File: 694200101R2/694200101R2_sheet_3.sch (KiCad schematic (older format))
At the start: 48 parts

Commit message: Updated Schematic to use KiCad LED Driver Symbols
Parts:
- added C18, C20, C21, C22: 0.47uF, Capacitor_SMD:C_0603_1608Metric, symbol Device:C
- added C19: 22uF, capacitor-lib:CAPPC3528X210N, symbol Device:CP1
- added C23, C24, C27: 100nF, Capacitor_SMD:C_0603_1608Metric, symbol Device:C
- added R11: 59k, Resistor_SMD:R_2512_6332Metric, symbol Device:R_US
- added R15, R16: 100k, Resistor_SMD:R_0603_1608Metric, symbol Device:R_US
- added U6: IS31FL3733-TQ, Package_QFP:TQFP-48-1EP_7x7mm_P0.5mm_EP5x5mm_ThermalVias, symbol cldg:IS31FL3733-TQ
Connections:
- net CS10_B: now also U6.26 (CS10)
- net CS11_B: now also U6.27 (CS11)
- net CS12_B: now also U6.28 (CS12)
- net CS1_B: now also U6.16 (CS1)
- net CS2_B: now also U6.17 (CS2)
- net CS3_B: now also U6.18 (CS3)
- net CS4_B: now also U6.19 (CS4)
- net CS5_B: now also U6.21 (CS5)
- net CS6_B: now also U6.22 (CS6)
- net CS7_B: now also U6.23 (CS7)
- net CS8_B: now also U6.24 (CS8)
- net CS9_B: now also U6.25 (CS9)
- net SW10_B: now also U6.13 (SW10)
- net SW11_B: now also U6.14 (SW11)
- net SW12_B: now also U6.15 (SW12)
- net SW1_B: now also U6.2 (SW1)
- net SW2_B: now also U6.3 (SW2)
- net SW3_B: now also U6.4 (SW3)
- net SW4_B: now also U6.6 (SW4)
- net SW5_B: now also U6.7 (SW5)
- net SW6_B: now also U6.8 (SW6)
- net SW7_B: now also U6.9 (SW7)
- net SW8_B: now also U6.10 (SW8)
- net SW9_B: now also U6.11 (SW9)
- new net: R15.1, U6.46 (~SDB)
- new net: R11.1, U6.35 (RSET)
- new net: R16.2, U6.47 (IICRST)
- new net +3V3: C18.1, R15.2, U6.39 (VIO)
- new net GND: C18.2, C19.2, C20.2, C21.2, C22.2, C23.2, C24.2, C27.2, R11.2, R16.1, U6.12 (PGND), U6.34 (AGND), U6.44 (ADDR2), U6.48 (GND), U6.49 (GND), U6.5 (PGND)
- new net I2C_SCL: U6.42 (SCL), U6.43 (ADDR1)
- new net I2C_SDA: U6.41 (SDA)
- new net SYNC: U6.40 (SYNC)
- new net VCC: C19.1, C20.1, C21.1, C22.1, C23.1, C24.1, C27.1, U6.20 (PVCC), U6.29 (PVCC), U6.37 (AVCC), U6.38 (DVCC)
- no-connect marks 0 -> 5
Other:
- note added: "LED Driver B - Addr"
- note added: "LED Driver B - Power Filtering"
- note added: "LED_DRIVER_B\nP20"
- note added: "LED_DRIVER_B\nP29"
- note added: "LED_DRIVER_B\nP37/38"
- note added: "LED_DRIVER_B\nPWR_FILTER"
- moved on the sheet: D173, D174, D175, D176, D177, D178, D179, D180, D181, D182, D183, D184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

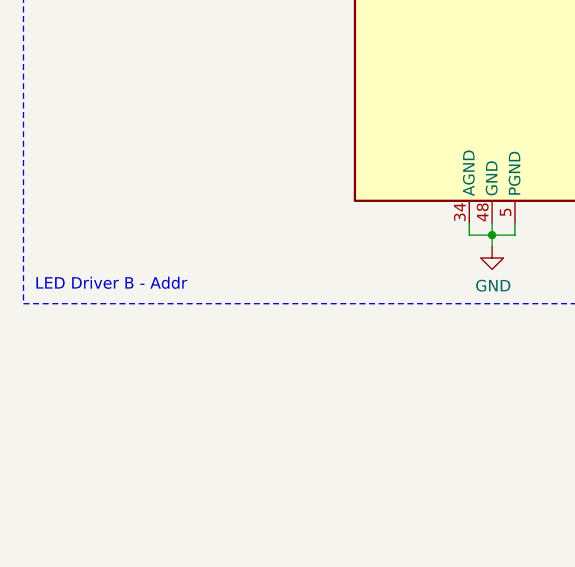
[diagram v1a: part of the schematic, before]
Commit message: Updated Address in schematic
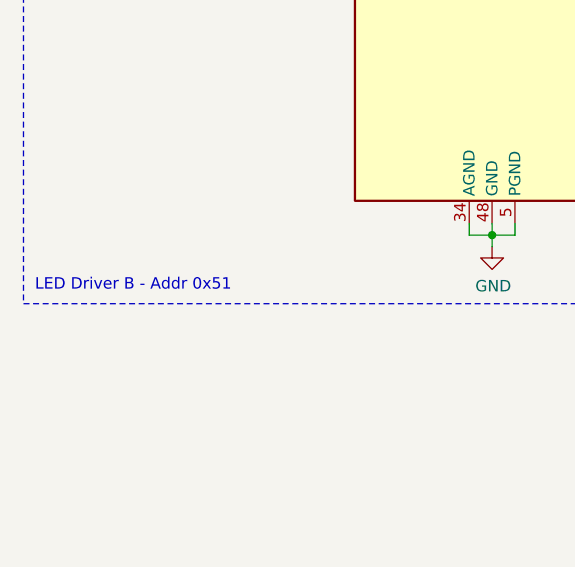
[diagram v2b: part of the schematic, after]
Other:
- note added: "LED Driver B - Addr 0x51"
- note removed: "LED Driver B - Addr"
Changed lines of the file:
@@
 	4200 7475 4200 3025
 Text Notes 900  7425 0    50   ~ 0
-LED Driver B - Addr
+LED Driver B - Addr 0x51
 Wire Notes Line
 	6925 3025 6925 7475

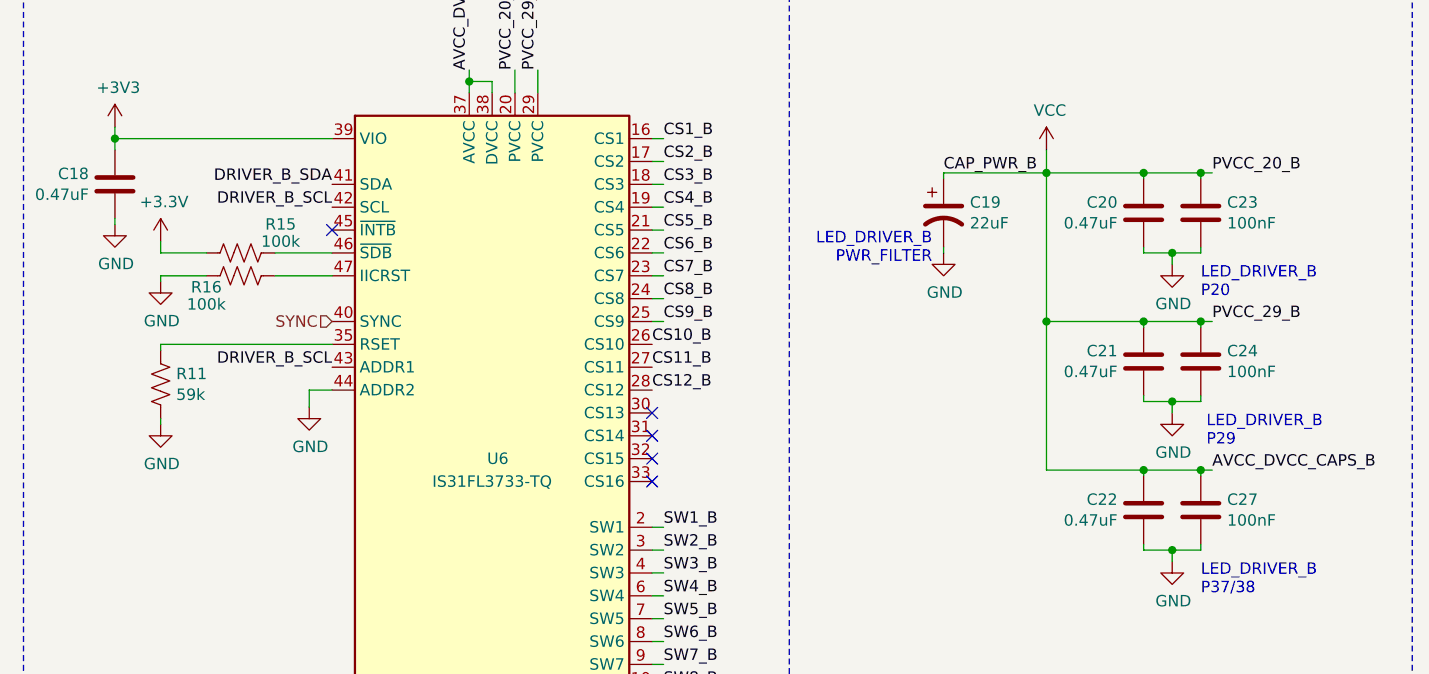
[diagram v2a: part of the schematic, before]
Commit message: Fixed Ratsnest errors from prettifying schematic
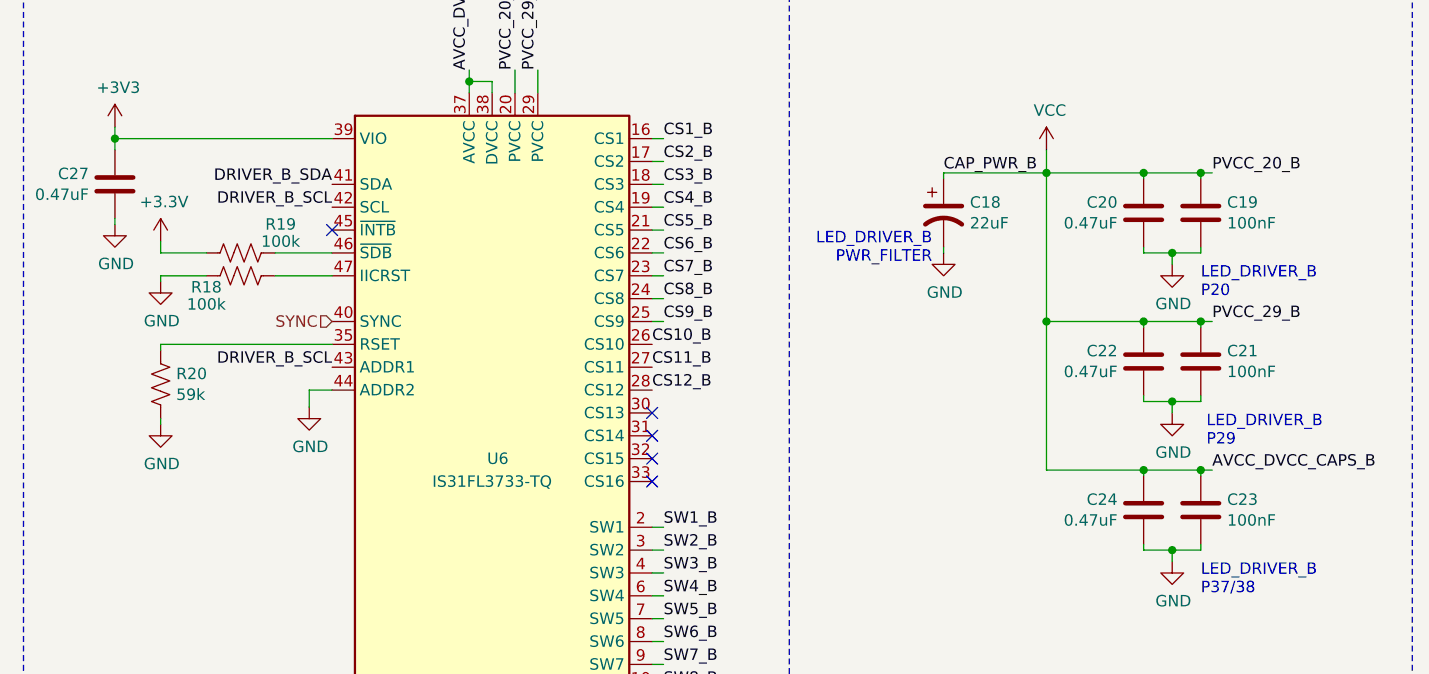
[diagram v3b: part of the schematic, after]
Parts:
- renumbered C19 to C18, C23 to C19, C24 to C21, C21 to C22, C27 to C23, C22 to C24, C18 to C27, R16 to R18, R15 to R19, R11 to R20
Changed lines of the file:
@@
 P 1250 4325
 AR Path="/63A35802/74967E57" Ref="C?"  Part="1"
-AR Path="/63A35802/6000FEDE/74967E57" Ref="C18"  Part="1"
-F 0 "C18" H 1136 4371 50  0000 R CNN
+AR Path="/63A35802/6000FEDE/74967E57" Ref="C27"  Part="1"
+F 0 "C27" H 1136 4371 50  0000 R CNN
 F 1 "0.47uF" H 1136 4280 50  0000 R CNN
 F 2 "Capacitor_SMD:C_0603_1608Metric" H 1288 4175 50  0001 C CNN
@@
 P 1800 4625
 AR Path="/63A35802/74967E75" Ref="R?"  Part="1"
-AR Path="/63A35802/6000FEDE/74967E75" Ref="R15"  Part="1"
-F 0 "R15" V 1675 4800 50  0000 C CNN
+AR Path="/63A35802/6000FEDE/74967E75" Ref="R19"  Part="1"
+F 0 "R19" V 1675 4800 50  0000 C CNN
 F 1 "100k" V 1750 4800 50  0000 C CNN
 F 2 "Resistor_SMD:R_0603_1608Metric" V 1840 4615 50  0001 C CNN
@@
 P 1450 5200
 AR Path="/63A35802/74967E83" Ref="R?"  Part="1"
-AR Path="/63A35802/6000FEDE/74967E83" Ref="R11"  Part="1"
-F 0 "R11" H 1518 5246 50  0000 L CNN
+AR Path="/63A35802/6000FEDE/74967E83" Ref="R20"  Part="1"
+F 0 "R20" H 1518 5246 50  0000 L CNN
 F 1 "59k" H 1518 5155 50  0000 L CNN
 F 2 "Resistor_SMD:R_2512_6332Metric" V 1490 5190 50  0001 C CNN
@@
 P 1800 4725
 AR Path="/63A35802/74967E89" Ref="R?"  Part="1"
-AR Path="/63A35802/6000FEDE/74967E89" Ref="R16"  Part="1"
-F 0 "R16" V 1750 4875 50  0000 C CNN
+AR Path="/63A35802/6000FEDE/74967E89" Ref="R18"  Part="1"
+F 0 "R18" V 1750 4875 50  0000 C CNN
 F 1 "100k" V 1675 4875 50  0000 C CNN
 F 2 "Resistor_SMD:R_0603_1608Metric" V 1840 4715 50  0001 C CNN
@@
 P 4875 4450
 AR Path="/63A35802/74967ED4" Ref="C?"  Part="1"
-AR Path="/63A35802/6000FEDE/74967ED4" Ref="C19"  Part="1"
-F 0 "C19" H 4990 4496 50  0000 L CNN
+AR Path="/63A35802/6000FEDE/74967ED4" Ref="C18"  Part="1"
+F 0 "C18" H 4990 4496 50  0000 L CNN
 F 1 "22uF" H 4990 4405 50  0000 L CNN
 F 2 "capacitor-lib:CAPPC3528X210N" H 4875 4450 50  0001 C CNN
@@
 P 6000 5100
 AR Path="/63A35802/74967EEB" Ref="C?"  Part="1"
-AR Path="/63A35802/6000FEDE/74967EEB" Ref="C24"  Part="1"
-F 0 "C24" H 6115 5146 50  0000 L CNN
+AR Path="/63A35802/6000FEDE/74967EEB" Ref="C21"  Part="1"
+F 0 "C21" H 6115 5146 50  0000 L CNN
 F 1 "100nF" H 6115 5055 50  0000 L CNN
 F 2 "Capacitor_SMD:C_0603_1608Metric" H 6038 4950 50  0001 C CNN
@@
 P 5750 5100
 AR Path="/63A35802/74967EF1" Ref="C?"  Part="1"
-AR Path="/63A35802/6000FEDE/74967EF1" Ref="C21"  Part="1"
-F 0 "C21" H 5636 5146 50  0000 R CNN
+AR Path="/63A35802/6000FEDE/74967EF1" Ref="C22"  Part="1"
+F 0 "C22" H 5636 5146 50  0000 R CNN
 F 1 "0.47uF" H 5636 5055 50  0000 R CNN
 F 2 "Capacitor_SMD:C_0603_1608Metric" H 5788 4950 50  0001 C CNN
@@
 P 6000 4450
 AR Path="/63A35802/74967F08" Ref="C?"  Part="1"
-AR Path="/63A35802/6000FEDE/74967F08" Ref="C23"  Part="1"
-F 0 "C23" H 6115 4496 50  0000 L CNN
+AR Path="/63A35802/6000FEDE/74967F08" Ref="C19"  Part="1"
+F 0 "C19" H 6115 4496 50  0000 L CNN
 F 1 "100nF" H 6115 4405 50  0000 L CNN
 F 2 "Capacitor_SMD:C_0603_1608Metric" H 6038 4300 50  0001 C CNN
@@
 P 6000 5750
 AR Path="/63A35802/74967F24" Ref="C?"  Part="1"
-AR Path="/63A35802/6000FEDE/74967F24" Ref="C27"  Part="1"
-F 0 "C27" H 6115 5796 50  0000 L CNN
+AR Path="/63A35802/6000FEDE/74967F24" Ref="C23"  Part="1"
+F 0 "C23" H 6115 5796 50  0000 L CNN
 F 1 "100nF" H 6115 5705 50  0000 L CNN
 F 2 "Capacitor_SMD:C_0603_1608Metric" H 6038 5600 50  0001 C CNN
@@
 P 5750 5750
 AR Path="/63A35802/74967F2A" Ref="C?"  Part="1"
-AR Path="/63A35802/6000FEDE/74967F2A" Ref="C22"  Part="1"
-F 0 "C22" H 5636 5796 50  0000 R CNN
+AR Path="/63A35802/6000FEDE/74967F2A" Ref="C24"  Part="1"
+F 0 "C24" H 5636 5796 50  0000 R CNN
 F 1 "0.47uF" H 5636 5705 50  0000 R CNN
 F 2 "Capacitor_SMD:C_0603_1608Metric" H 5788 5600 50  0001 C CNN

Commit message: Updated Footprints to have CAD Models
Need footprints on board to allow for case modifications
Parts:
- C18: footprint capacitor-lib:CAPPC3528X210N -> Capacitor_Tantalum_SMD:CP_EIA-3528-21_Kemet-B
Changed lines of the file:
@@
 F 0 "C18" H 4990 4496 50  0000 L CNN
 F 1 "22uF" H 4990 4405 50  0000 L CNN
-F 2 "capacitor-lib:CAPPC3528X210N" H 4875 4450 50  0001 C CNN
+F 2 "Capacitor_Tantalum_SMD:CP_EIA-3528-21_Kemet-B" H 4875 4450 50  0001 C CNN
 F 3 "~" H 4875 4450 50  0001 C CNN
 	1    4875 4450
